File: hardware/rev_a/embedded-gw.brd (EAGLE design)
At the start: 38.5 x 55.5 mm, 49 parts, among them J1 DM3BT-DSF-PEJS, J2 TC2030-JLINK-NL, J3 USB-A-MALE-PLUG, U1 AP7362A-33SP-13, U2 BT840X, U3 CP2102N-20, U4 ESDR0502N, U5 ESP32-WROVER-E, U6 ESP32-WROVER-E, X1 ABS05-32.768KHZ-9-T

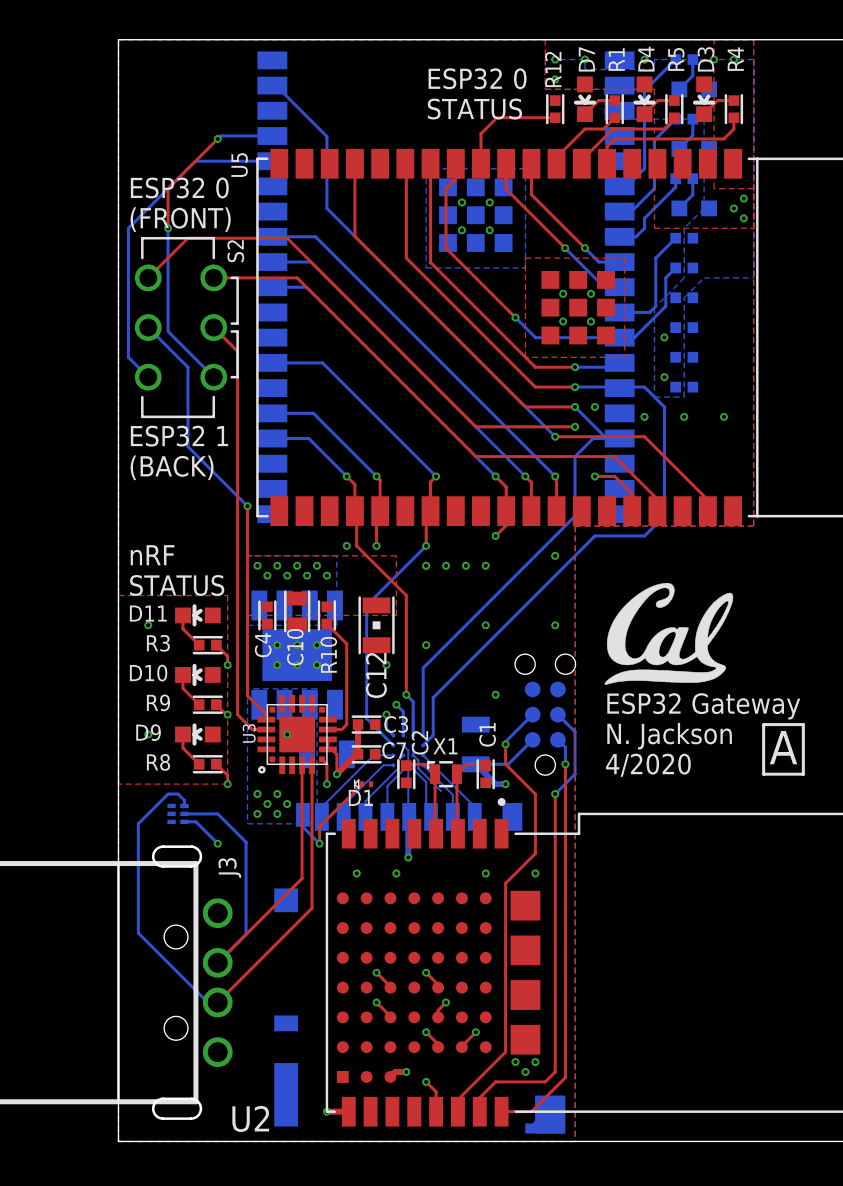
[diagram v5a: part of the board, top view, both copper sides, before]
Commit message: leave gpio12 floating, add diode
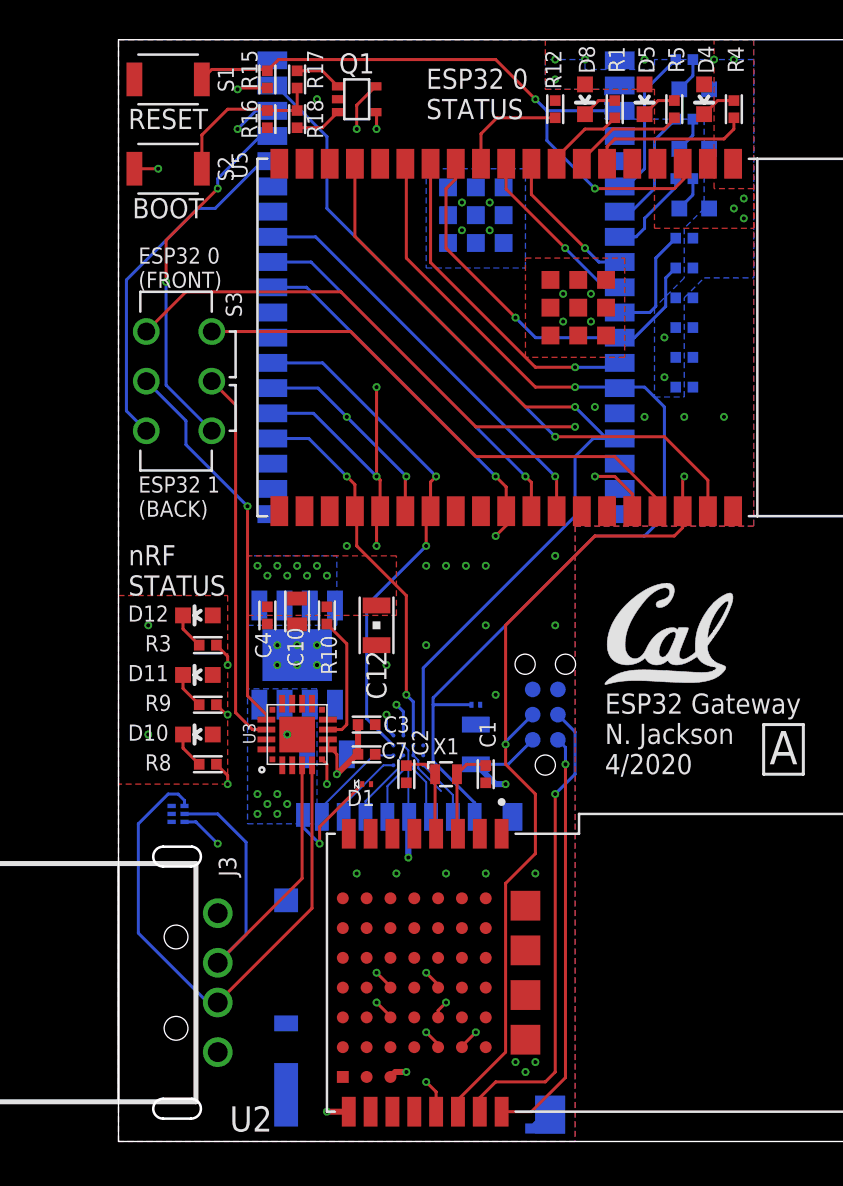
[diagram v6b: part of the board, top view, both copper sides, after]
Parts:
- added D12: BLUE, leds:LED-0603
- added Q1: DMN32D2LDF, fets:SOT353
- added R15, R16: 10k, passives:0402_RES
- added R17, R18: 1k, passives:0402_RES
- added S1: B3U-1000P, switches:B3U-1000P
- added S3: JS202011CQN, switches:JS202011CQN
- D10, D4, D6: value YELLOW -> RED
- D11, D7: value BLUE -> YELLOW
- D2: value EMIF06-MSD01F2 -> (none); device passives:BGA16C50P4X4_192X192X65N -> passives:0201_DIODE
- D3: value RED -> EMIF06-MSD01F2; device leds:LED-0603 -> passives:BGA16C50P4X4_192X192X65N
- D5: value RED -> YELLOW
- D9: value RED -> BLUE
- S2: value JS202011CQN -> B3U-1000P; device switches:JS202011CQN -> switches:B3U-1000P
- moved D9 36.4 mm to (29.0, 47.0), flipped to the bottom, turned to 270 degrees
- moved D3 36.0 mm to (14.6, 19.7), flipped to the bottom, turned to 270 degrees
- moved D8 7.78 mm to (23.5, 52.5), flipped to the top, turned to 180 degrees
- moved D7 6.04 mm to (29.0, 50.0), flipped to the bottom, turned to 270 degrees
- moved S2 5.59 mm to (2.50, 49.0), turned to 0 degrees
- moved D2 4.10 mm to (18.0, 22.0)
- moved D10 3.00 mm to (4.00, 20.5)
- moved D11 3.00 mm to (4.00, 23.5)
- moved D4 3.00 mm to (29.5, 52.5)
- moved D6 3.00 mm to (29.0, 53.0)
- moved D5 2.55 mm to (26.5, 52.5), flipped to the top, turned to 180 degrees
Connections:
- removed net !RESET: J2.3, U2.14
- removed net N$10: D2.D3, J1.1
- new net !NRF_RESET: J2.3, U2.14, U5.36, U6.36
- new net EN: R15.1, S1.2, U5.3, U6.3
- new net IO0: Q1.D1, U5.25, U6.25
- new net N$1: Q1.G1, R17.2
- new net N$4: Q1.G2, R18.2
- new net N$5: R16.2, R17.1, R18.1, S2.2
- net ESP32_0_RXD: now also S3.1; no longer S2.1
- net ESP32_0_TXD: now also S3.4; no longer S2.4
- net ESP32_1_RXD: now also S3.3; no longer S2.3
- net ESP32_1_TXD: now also S3.6; no longer S2.6
- net GND: now also D2.P$2, D3.B3, D3.C2, D3.C3, Q1.S, R16.1, S1.1; no longer D2.B3, D2.C2, D2.C3
- net N$11: now also D3.D4; no longer D2.D4
- net N$12: now also D4.C; no longer D3.C
- net N$13: now also D3.B4; no longer D2.B4
- net N$14: now also D5.C; no longer D4.C
- net N$15: now also D8.C; no longer D7.C
- net N$19: now also D6.C; no longer D5.C
- net N$20: now also D7.C; no longer D6.C
- net N$21: now also D9.C; no longer D8.C
- net N$22: now also D10.C; no longer D9.C
- net N$23: now also D11.C; no longer D10.C
- net N$24: now also D12.C; no longer D11.C
- net N$6: now also D3.C4; no longer D2.C4
- net N$8: now also D3.A4; no longer D2.A4
- net N$9: now also D3.A3; no longer D2.A3
- net RXD: now also S3.2; no longer S2.2
- net SD_HOST_CLK: now also D3.B1; no longer D2.B1
- net SD_HOST_CMD: now also D3.C1; no longer D2.C1
- net SD_HOST_D0: now also D3.A1, Q1.D2; no longer D2.A1
- net SD_HOST_D1: now also D3.A2; no longer D2.A2
- net SD_HOST_D2: now also D2.P$1, J1.1; no longer D2.D2
- net SD_HOST_D3: now also D3.D1; no longer D2.D1
- net TXD: now also S3.5; no longer S2.5
- net VCC: now also D12.A, D3.B2, R15.2, S2.1; no longer D2.B2, D3.A, U5.3, U6.3
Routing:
- net !NRF_RESET: track 0.00 -> 81.5 mm, vias 0 -> 3
- net EN: track 0.00 -> 33.0 mm, vias 0 -> 2
- net IO0: track 0.00 -> 27.6 mm, vias 0 -> 3
- net !RESET: track 22.8 -> 0.00 mm, vias 1 -> 0
- net SD_HOST_D0: track 20.1 -> 38.5 mm, vias 3 -> 5
- net N$5: track 0.00 -> 8.20 mm
- net SD_HOST_D2: track 44.5 -> 50.7 mm
- net N$10: track 4.17 -> 0.00 mm
- net VCC: track 14.4 -> 17.2 mm, vias 24 -> 26
- net TXD: track 21.8 -> 19.1 mm
- net RXD: track 22.2 -> 19.6 mm
- net N$4: track 0.00 -> 2.37 mm
- net N$1: track 0.00 -> 2.37 mm
- net ESP32_1_TXD: track 16.8 -> 18.4 mm
- net ESP32_1_RXD: track 16.6 -> 17.8 mm
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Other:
- board text added: "BOOT"
- board text added: "RESET"
